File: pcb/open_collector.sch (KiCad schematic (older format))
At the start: 44 parts, among them Q1 BC817, Q2 BC817, Q3 BC817, Q4 BC817, Q5 BC817, Q6 BC817

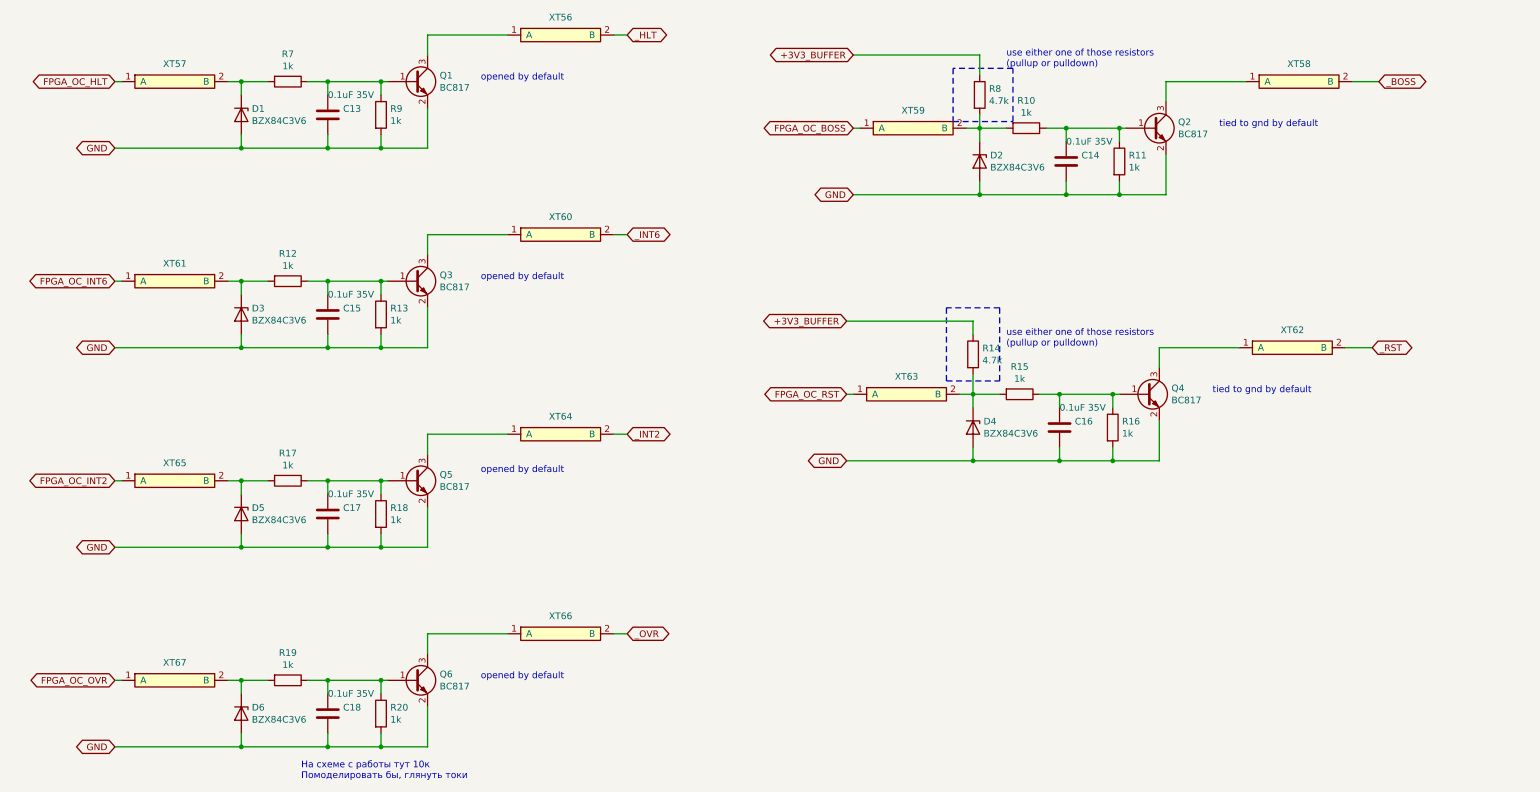
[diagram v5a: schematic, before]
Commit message: Buffers power scheme rework in progress, re-annotate board
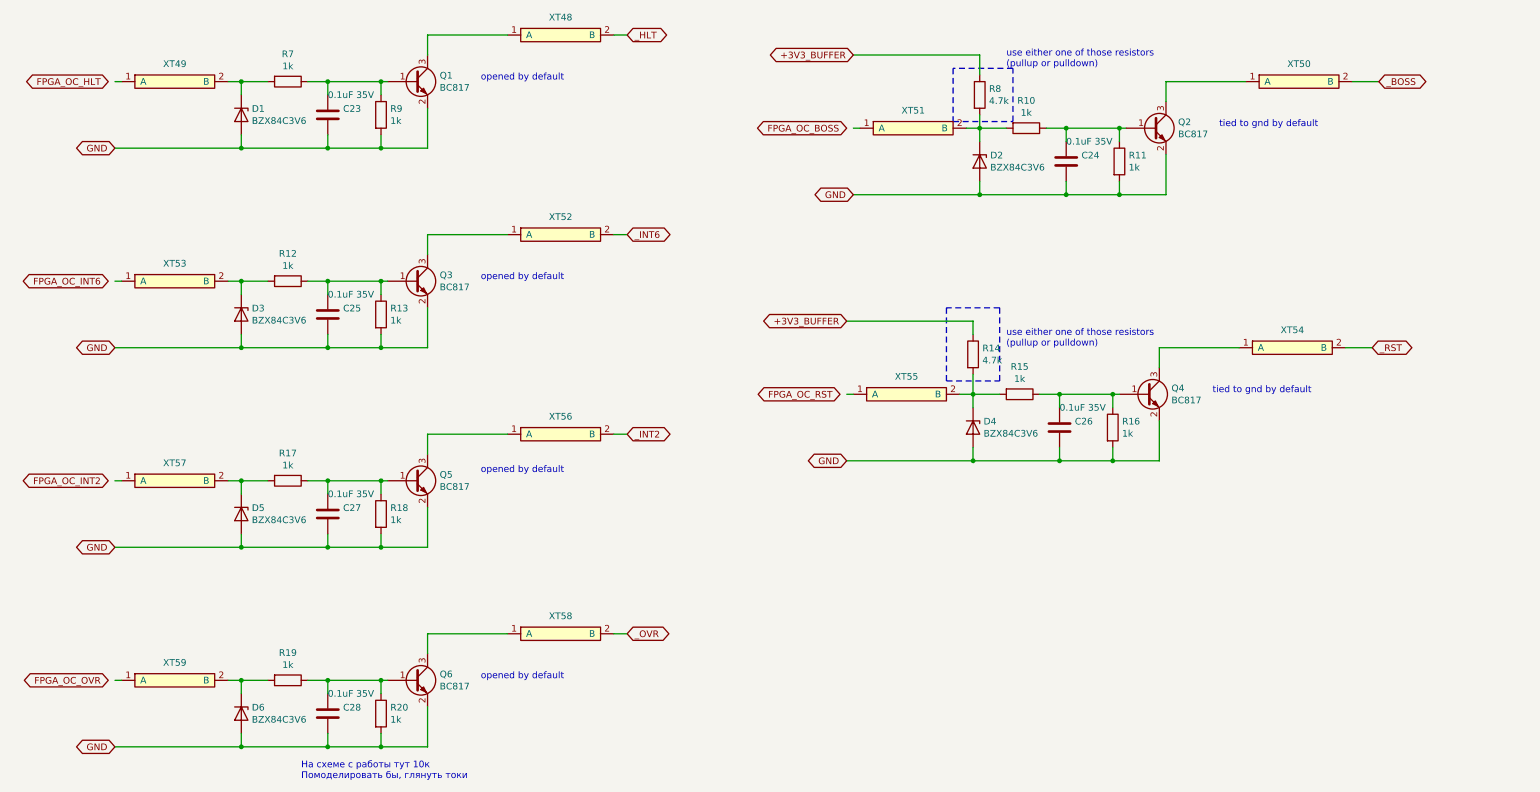
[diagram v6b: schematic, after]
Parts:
- renumbered C13 to C23, C14 to C24, C15 to C25, C16 to C26, C17 to C27, C18 to C28, XT56 to XT48, XT57 to XT49, XT58 to XT50, XT59 to XT51, XT60 to XT52, XT61 to XT53, XT62 to XT54, XT63 to XT55, XT64 to XT56, XT65 to XT57, XT66 to XT58, XT67 to XT59
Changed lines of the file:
@@
 Text GLabel 1150 6500 0    50   BiDi ~ 0
 GND
-Text GLabel 6700 1850 0    50   BiDi ~ 0
+Text GLabel 6650 1850 0    50   BiDi ~ 0
 FPGA_OC_BOSS
-Text GLabel 6650 3850 0    50   BiDi ~ 0
+Text GLabel 6600 3850 0    50   BiDi ~ 0
 FPGA_OC_RST
-Text GLabel 1150 1500 0    50   BiDi ~ 0
+Text GLabel 1100 1500 0    50   BiDi ~ 0
 FPGA_OC_HLT
-Text GLabel 1150 3000 0    50   BiDi ~ 0
+Text GLabel 1100 3000 0    50   BiDi ~ 0
 FPGA_OC_INT6
-Text GLabel 1150 4500 0    50   BiDi ~ 0
+Text GLabel 1100 4500 0    50   BiDi ~ 0
 FPGA_OC_INT2
-Text GLabel 1150 6000 0    50   BiDi ~ 0
+Text GLabel 1100 6000 0    50   BiDi ~ 0
 FPGA_OC_OVR
-Text GLabel 10600 3500 2    50   BiDi ~ 0
-_RST
-Text GLabel 5000 1150 2    50   BiDi ~ 0
-_HLT
-Text GLabel 5000 2650 2    50   BiDi ~ 0
-_INT6
-Text GLabel 5000 4150 2    50   BiDi ~ 0
-_INT2
-Text GLabel 5000 5650 2    50   BiDi ~ 0
-_OVR
-$Comp
-L WM1200:testpoint_cutline XT67
+$Comp
+L WM1200:testpoint_cutline XT59
 U 1 1 5E66C58B
 P 1600 6050
-F 0 "XT67" H 1600 6233 50  0000 C CNN
+F 0 "XT59" H 1600 6233 50  0000 C CNN
 F 1 "testpoint_cutline" H 1600 6200 50  0001 C CNN
 F 2 "WM1200:testpoint_cutline" H 1750 6050 50  0001 C CNN
@@
 $EndComp
 $Comp
-L WM1200:testpoint_cutline XT65
+L WM1200:testpoint_cutline XT57
 U 1 1 5E66D323
 P 1600 4550
-F 0 "XT65" H 1600 4733 50  0000 C CNN
+F 0 "XT57" H 1600 4733 50  0000 C CNN
 F 1 "testpoint_cutline" H 1600 4700 50  0001 C CNN
 F 2 "WM1200:testpoint_cutline" H 1750 4550 50  0001 C CNN
@@
 $EndComp
 $Comp
-L WM1200:testpoint_cutline XT61
+L WM1200:testpoint_cutline XT53
 U 1 1 5E66DA82
 P 1600 3050
-F 0 "XT61" H 1600 3233 50  0000 C CNN
+F 0 "XT53" H 1600 3233 50  0000 C CNN
 F 1 "testpoint_cutline" H 1600 3200 50  0001 C CNN
 F 2 "WM1200:testpoint_cutline" H 1750 3050 50  0001 C CNN
@@
 $EndComp
 $Comp
-L WM1200:testpoint_cutline XT57
+L WM1200:testpoint_cutline XT49
 U 1 1 5E66DF74
 P 1600 1550
-F 0 "XT57" H 1600 1733 50  0000 C CNN
+F 0 "XT49" H 1600 1733 50  0000 C CNN
 F 1 "testpoint_cutline" H 1600 1700 50  0001 C CNN
 F 2 "WM1200:testpoint_cutline" H 1750 1550 50  0001 C CNN
@@
 $EndComp
 $Comp
-L WM1200:testpoint_cutline XT63
+L WM1200:testpoint_cutline XT55
 U 1 1 5E66E467
 P 7100 3900
-F 0 "XT63" H 7100 4083 50  0000 C CNN
+F 0 "XT55" H 7100 4083 50  0000 C CNN
 F 1 "testpoint_cutline" H 7100 4050 50  0001 C CNN
 F 2 "WM1200:testpoint_cutline" H 7250 3900 50  0001 C CNN
@@
 $EndComp
 $Comp
-L WM1200:testpoint_cutline XT59
+L WM1200:testpoint_cutline XT51
 U 1 1 5E66EAB6
 P 7150 1900
-F 0 "XT59" H 7150 2083 50  0000 C CNN
+F 0 "XT51" H 7150 2083 50  0000 C CNN
 F 1 "testpoint_cutline" H 7150 2050 50  0001 C CNN
 F 2 "WM1200:testpoint_cutline" H 7300 1900 50  0001 C CNN
@@
 	2000 6000 2100 6000
 Connection ~ 2100 6000
-Text GLabel 10650 1500 2    50   BiDi ~ 0
-_BOSS
-$Comp
-L WM1200:testpoint_cutline XT66
+$Comp
+L WM1200:testpoint_cutline XT58
 U 1 1 5E5E18CC
 P 4500 5700
-F 0 "XT66" H 4500 5883 50  0000 C CNN
+F 0 "XT58" H 4500 5883 50  0000 C CNN
 F 1 "testpoint_cutline" H 4500 5850 50  0001 C CNN
 F 2 "WM1200:testpoint_cutline" H 4650 5700 50  0001 C CNN
@@
 $EndComp
 $Comp
-L WM1200:testpoint_cutline XT64
+L WM1200:testpoint_cutline XT56
 U 1 1 5E5E2E8F
 P 4500 4200
-F 0 "XT64" H 4500 4383 50  0000 C CNN
+F 0 "XT56" H 4500 4383 50  0000 C CNN
 F 1 "testpoint_cutline" H 4500 4350 50  0001 C CNN
 F 2 "WM1200:testpoint_cutline" H 4650 4200 50  0001 C CNN
@@
 $EndComp
 $Comp
-L WM1200:testpoint_cutline XT60
+L WM1200:testpoint_cutline XT52
 U 1 1 5E5E4469
 P 4500 2700
-F 0 "XT60" H 4500 2883 50  0000 C CNN
+F 0 "XT52" H 4500 2883 50  0000 C CNN
 F 1 "testpoint_cutline" H 4500 2850 50  0001 C CNN
 F 2 "WM1200:testpoint_cutline" H 4650 2700 50  0001 C CNN
@@
 $EndComp
 $Comp
-L WM1200:testpoint_cutline XT56
+L WM1200:testpoint_cutline XT48
 U 1 1 5E5E4F3D
 P 4500 1200
-F 0 "XT56" H 4500 1383 50  0000 C CNN
+F 0 "XT48" H 4500 1383 50  0000 C CNN
 F 1 "testpoint_cutline" H 4500 1350 50  0001 C CNN
 F 2 "WM1200:testpoint_cutline" H 4650 1200 50  0001 C CNN
@@
 $EndComp
 $Comp
-L WM1200:testpoint_cutline XT62
+L WM1200:testpoint_cutline XT54
 U 1 1 5E5E75D9
 P 10000 3550
-F 0 "XT62" H 10000 3733 50  0000 C CNN
+F 0 "XT54" H 10000 3733 50  0000 C CNN
 F 1 "testpoint_cutline" H 10000 3700 50  0001 C CNN
 F 2 "WM1200:testpoint_cutline" H 10150 3550 50  0001 C CNN
@@
 $EndComp
 $Comp
-L WM1200:testpoint_cutline XT58
+L WM1200:testpoint_cutline XT50
 U 1 1 5E5E7EC3
 P 10050 1550
-F 0 "XT58" H 10050 1733 50  0000 C CNN
+F 0 "XT50" H 10050 1733 50  0000 C CNN
 F 1 "testpoint_cutline" H 10050 1700 50  0001 C CNN
 F 2 "WM1200:testpoint_cutline" H 10200 1550 50  0001 C CNN
@@
 Connection ~ 8650 3850
 $Comp
-L Device:C C13
+L Device:C C23
 U 1 1 5E62A871
 P 2750 1750
-F 0 "C13" H 2635 1704 50  0000 R CNN
+F 0 "C23" H 2635 1704 50  0000 R CNN
 F 1 "0.1uF 35V" H 2750 1600 50  0000 R CNN
 F 2 "Capacitor_SMD:C_0603_1608Metric_Pad1.05x0.95mm_HandSolder" H 2788 1600 50  0001 C CNN
@@
 $EndComp
 $Comp
-L Device:C C15
+L Device:C C25
 U 1 1 5E62C766
 P 2750 3250
-F 0 "C15" H 2635 3204 50  0000 R CNN
+F 0 "C25" H 2635 3204 50  0000 R CNN
 F 1 "0.1uF 35V" H 2750 3100 50  0000 R CNN
 F 2 "Capacitor_SMD:C_0603_1608Metric_Pad1.05x0.95mm_HandSolder" H 2788 3100 50  0001 C CNN
@@
 $EndComp
 $Comp
-L Device:C C17
+L Device:C C27
 U 1 1 5E62F867
 P 2750 4750
-F 0 "C17" H 2635 4704 50  0000 R CNN
+F 0 "C27" H 2635 4704 50  0000 R CNN
 F 1 "0.1uF 35V" H 2750 4600 50  0000 R CNN
 F 2 "Capacitor_SMD:C_0603_1608Metric_Pad1.05x0.95mm_HandSolder" H 2788 4600 50  0001 C CNN
@@
 $EndComp
 $Comp
-L Device:C C18
+L Device:C C28
 U 1 1 5E632749
 P 2750 6250
-F 0 "C18" H 2635 6204 50  0000 R CNN
+F 0 "C28" H 2635 6204 50  0000 R CNN
 F 1 "0.1uF 35V" H 2750 6100 50  0000 R CNN
 F 2 "Capacitor_SMD:C_0603_1608Metric_Pad1.05x0.95mm_HandSolder" H 2788 6100 50  0001 C CNN
@@
 $EndComp
 $Comp
-L Device:C C16
+L Device:C C26
 U 1 1 5E635911
 P 8250 4100
-F 0 "C16" H 8135 4054 50  0000 R CNN
+F 0 "C26" H 8135 4054 50  0000 R CNN
 F 1 "0.1uF 35V" H 8250 3950 50  0000 R CNN
 F 2 "Capacitor_SMD:C_0603_1608Metric_Pad1.05x0.95mm_HandSolder" H 8288 3950 50  0001 C CNN
@@
 $EndComp
 $Comp
-L Device:C C14
+L Device:C C24
 U 1 1 5E6388BA
 P 8300 2100
-F 0 "C14" H 8185 2054 50  0000 R CNN
+F 0 "C24" H 8185 2054 50  0000 R CNN
 F 1 "0.1uF 35V" H 8300 1950 50  0000 R CNN
 F 2 "Capacitor_SMD:C_0603_1608Metric_Pad1.05x0.95mm_HandSolder" H 8338 1950 50  0001 C CNN
@@
 	0    1    1    0
 $EndComp
+Text GLabel 10650 1500 2    50   BiDi ~ 0
+_BOSS
+Text GLabel 10600 3500 2    50   BiDi ~ 0
+_RST
+Text GLabel 5000 5650 2    50   BiDi ~ 0
+_OVR
+Text GLabel 5000 4150 2    50   BiDi ~ 0
+_INT2
+Text GLabel 5000 2650 2    50   BiDi ~ 0
+_INT6
+Text GLabel 5000 1150 2    50   BiDi ~ 0
+_HLT
 $EndSCHEMATC

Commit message: time to stop for today
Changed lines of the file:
@@
 Text GLabel 1150 6500 0    50   BiDi ~ 0
 GND
-Text GLabel 6650 1850 0    50   BiDi ~ 0
+Text GLabel 6700 1850 0    50   BiDi ~ 0
 FPGA_OC_BOSS
-Text GLabel 6600 3850 0    50   BiDi ~ 0
+Text GLabel 6650 3850 0    50   BiDi ~ 0
 FPGA_OC_RST
-Text GLabel 1100 1500 0    50   BiDi ~ 0
+Text GLabel 1150 1500 0    50   BiDi ~ 0
 FPGA_OC_HLT
-Text GLabel 1100 3000 0    50   BiDi ~ 0
+Text GLabel 1150 3000 0    50   BiDi ~ 0
 FPGA_OC_INT6
-Text GLabel 1100 4500 0    50   BiDi ~ 0
+Text GLabel 1150 4500 0    50   BiDi ~ 0
 FPGA_OC_INT2
-Text GLabel 1100 6000 0    50   BiDi ~ 0
+Text GLabel 1150 6000 0    50   BiDi ~ 0
 FPGA_OC_OVR
 $Comp
